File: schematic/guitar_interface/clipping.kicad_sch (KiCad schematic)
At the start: 26 parts, among them IC3 LTC1440IS8#TRPBF, Q1 FDV301N, U5 OPA4134, U6 OPA4134

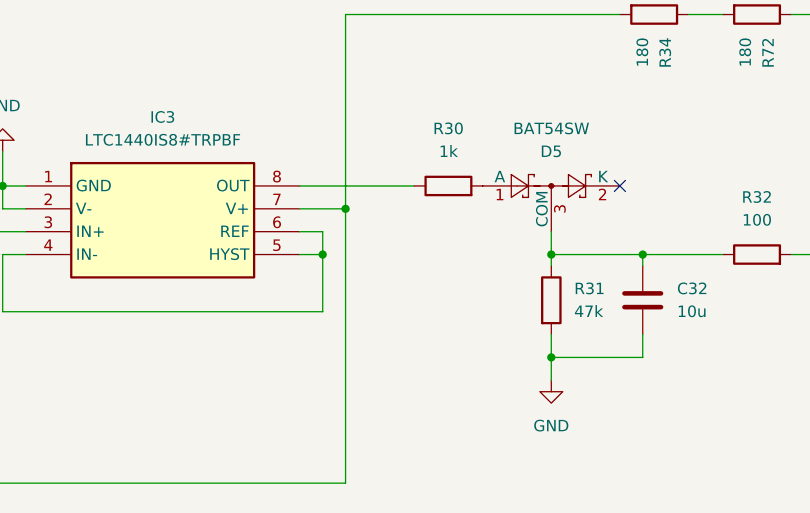
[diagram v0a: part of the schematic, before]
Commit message: refine layout fix, fix some minor issues, add additional ground planes on all layers, and add mounting holes
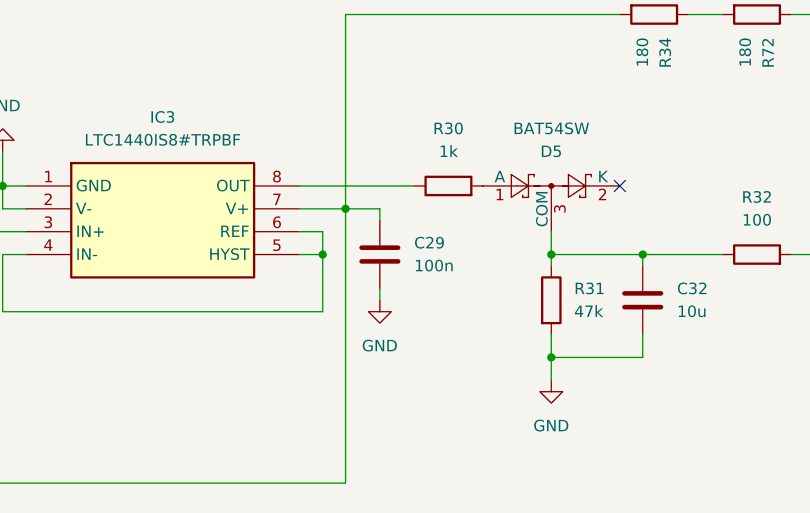
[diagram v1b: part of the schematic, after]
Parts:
- added C29: 100n, Capacitor_SMD:C_0402_1005Metric_Pad0.74x0.62mm_HandSolder, symbol Device:C
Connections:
- net GND: now also C29.2
- net VPP_3.3V: now also C29.1
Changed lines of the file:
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@@
+	(wire
+		(pts
+			(xy 151.13 137.16) (xy 151.13 138.43)
+		)
+		(stroke
+			(width 0)
+			(type default)
+		)
+	)
 	(wire
 		(pts
@@
 	(wire
 		(pts
+			(xy 151.13 129.54) (xy 151.13 128.27)
+		)
+		(stroke
+			(width 0)
+			(type default)
+		)
+	)
+	(wire
+		(pts
 			(xy 69.85 69.85) (xy 73.66 69.85)
 		)
@@
 		(pts
 			(xy 170.18 144.78) (xy 180.34 144.78)
+		)
+		(stroke
+			(width 0)
+			(type default)
+		)
+	)
+	(wire
+		(pts
+			(xy 147.32 128.27) (xy 151.13 128.27)
 		)
 		(stroke
@@
 	)
 	(symbol
+		(lib_id "Device:C")
+		(at 151.13 133.35 0)
+		(unit 1)
+		(exclude_from_sim no)
+		(in_bom yes)
+		(on_board yes)
+		(dnp no)
+		(fields_autoplaced yes)
+		(property "Reference" "C29"
+			(at 154.94 132.0799 0)
+			(effects
+				(font
+					(size 1.27 1.27)
+				)
+				(justify left)
+			)
+		)
+		(property "Value" "100n"
+			(at 154.94 134.6199 0)
+			(effects
+				(font
+					(size 1.27 1.27)
+				)
+				(justify left)
+			)
+		)
+		(property "Footprint" "Capacitor_SMD:C_0402_1005Metric_Pad0.74x0.62mm_HandSolder"
+			(at 152.0952 137.16 0)
+			(effects
+				(font
+					(size 1.27 1.27)
+				)
+				(hide yes)
+			)
+		)
+		(property "Datasheet" "~"
+			(at 151.13 133.35 0)
+			(effects
+				(font
+					(size 1.27 1.27)
+				)
+				(hide yes)
+			)
+		)
+		(property "Description" "Unpolarized capacitor"
+			(at 151.13 133.35 0)
+			(effects
+				(font
+					(size 1.27 1.27)
+				)
+				(hide yes)
+			)
+		)
+		(pin "1"
+		)
+		(pin "2"
+		)
+		(instances
+			(project ""
+				(path "/b77251ff-4eed-421f-8c84-983bb16b8e4c/06196554-bdb9-4f3b-8d58-477ce90b40ff"
+					(reference "C29")
+					(unit 1)
+				)
+			)
+		)
+	)
+	(symbol
 		(lib_id "Device:R")
 		(at 170.18 138.43 0)
@@
 					(unit 1)
 				)
+			)
+		)
+	)
+	(symbol
+		(lib_id "power:GND")
+		(at 151.13 138.43 0)
+		(unit 1)
+		(exclude_from_sim no)
+		(in_bom yes)
+		(on_board yes)
+		(dnp no)
+		(fields_autoplaced yes)
+		(property "Reference" "#PWR061"
+			(at 151.13 144.78 0)
+			(effects
+				(font
+					(size 1.27 1.27)
+				)
+				(hide yes)
+			)
+		)
+		(property "Value" "GND"
+			(at 151.13 143.51 0)
+			(effects
+				(font
+					(size 1.27 1.27)
+				)
+			)
+		)
+		(property "Footprint" ""
+			(at 151.13 138.43 0)
+			(effects
+				(font
+					(size 1.27 1.27)
+				)
+				(hide yes)
+			)
+		)
+		(property "Datasheet" ""
+			(at 151.13 138.43 0)
+			(effects
+				(font
+					(size 1.27 1.27)
+				)
+				(hide yes)
+			)
+		)
+		(property "Description" "Power symbol creates a global label with name \"GND\" , ground"
+			(at 151.13 138.43 0)
+			(effects
+				(font
+					(size 1.27 1.27)
+				)
+				(hide yes)
+			)
+		)
+		(pin "1"
+		)
+		(instances
+			(project ""
+				(path "/b77251ff-4eed-421f-8c84-983bb16b8e4c/06196554-bdb9-4f3b-8d58-477ce90b40ff"
+					(reference "#PWR061")
+					(unit 1)
+				)
